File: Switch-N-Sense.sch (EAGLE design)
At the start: 40 parts, among them Q1 ZXMP10A13F, Q2 FDMT80080DC, Q3 FDMT80080DC, Q4 FDMT80080DC, Q5 FDMT80080DC, U1 BQ76200

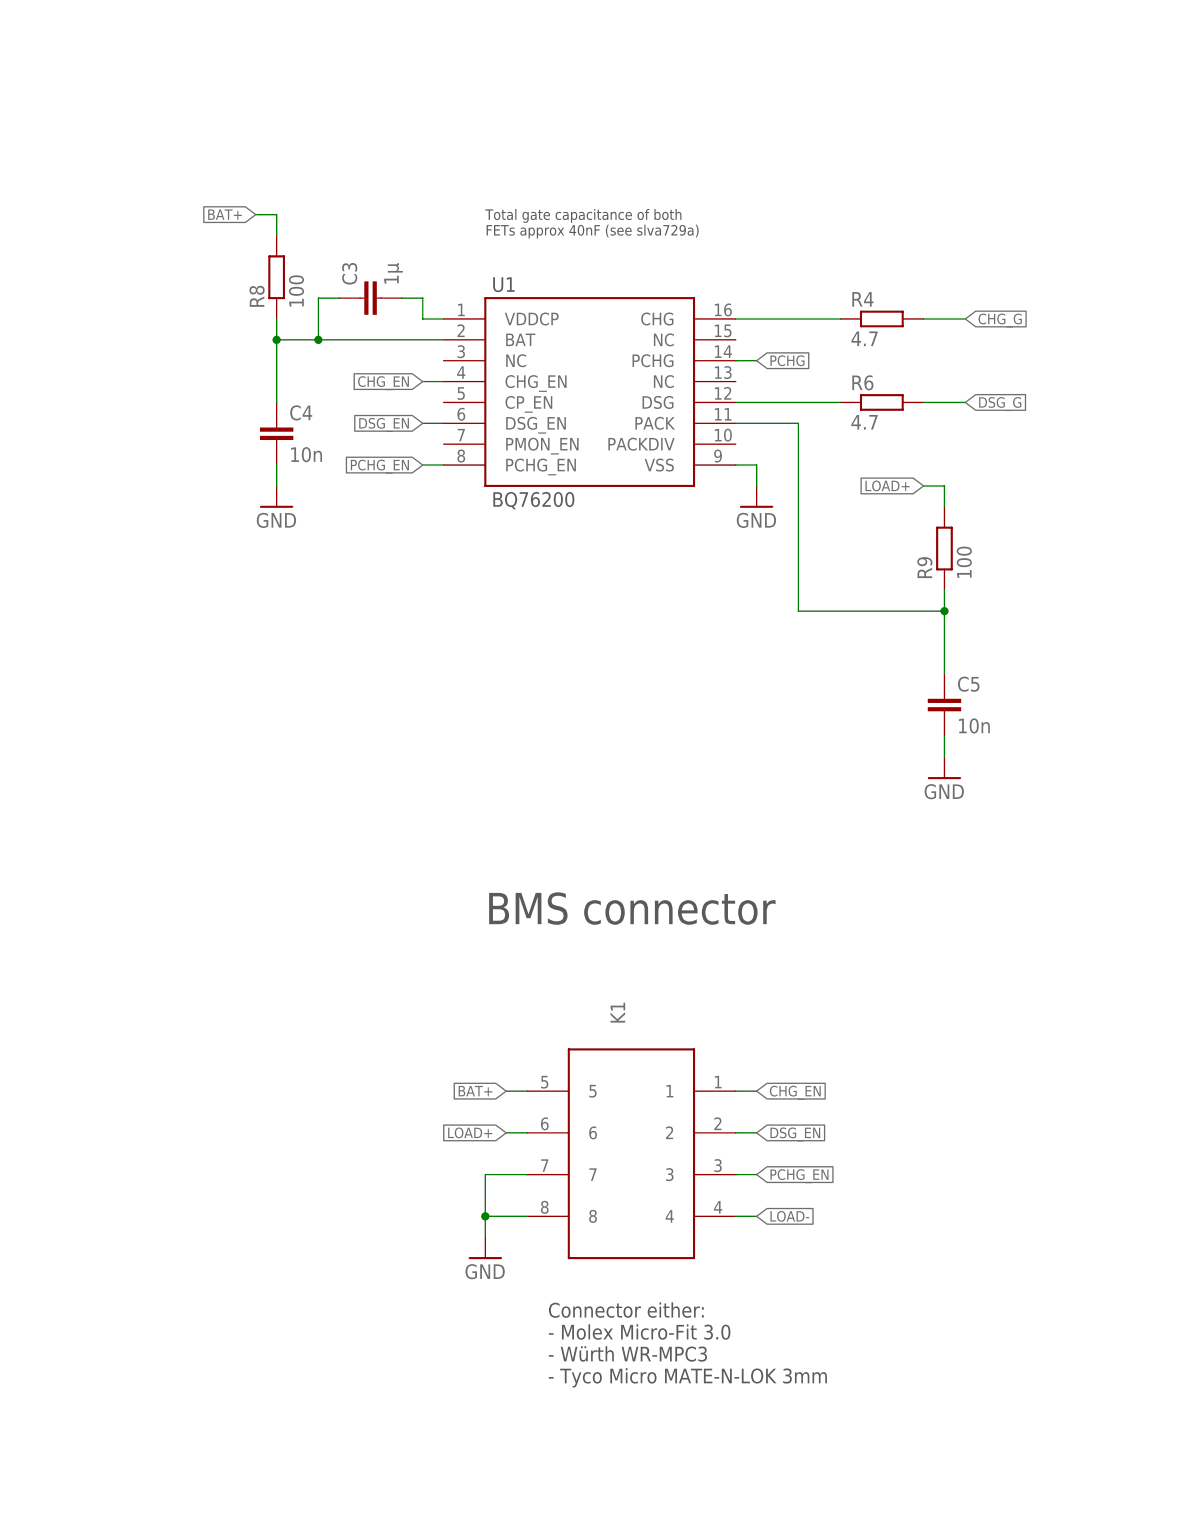
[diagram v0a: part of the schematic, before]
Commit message: Update to mate with new LibreSolar BMS48V
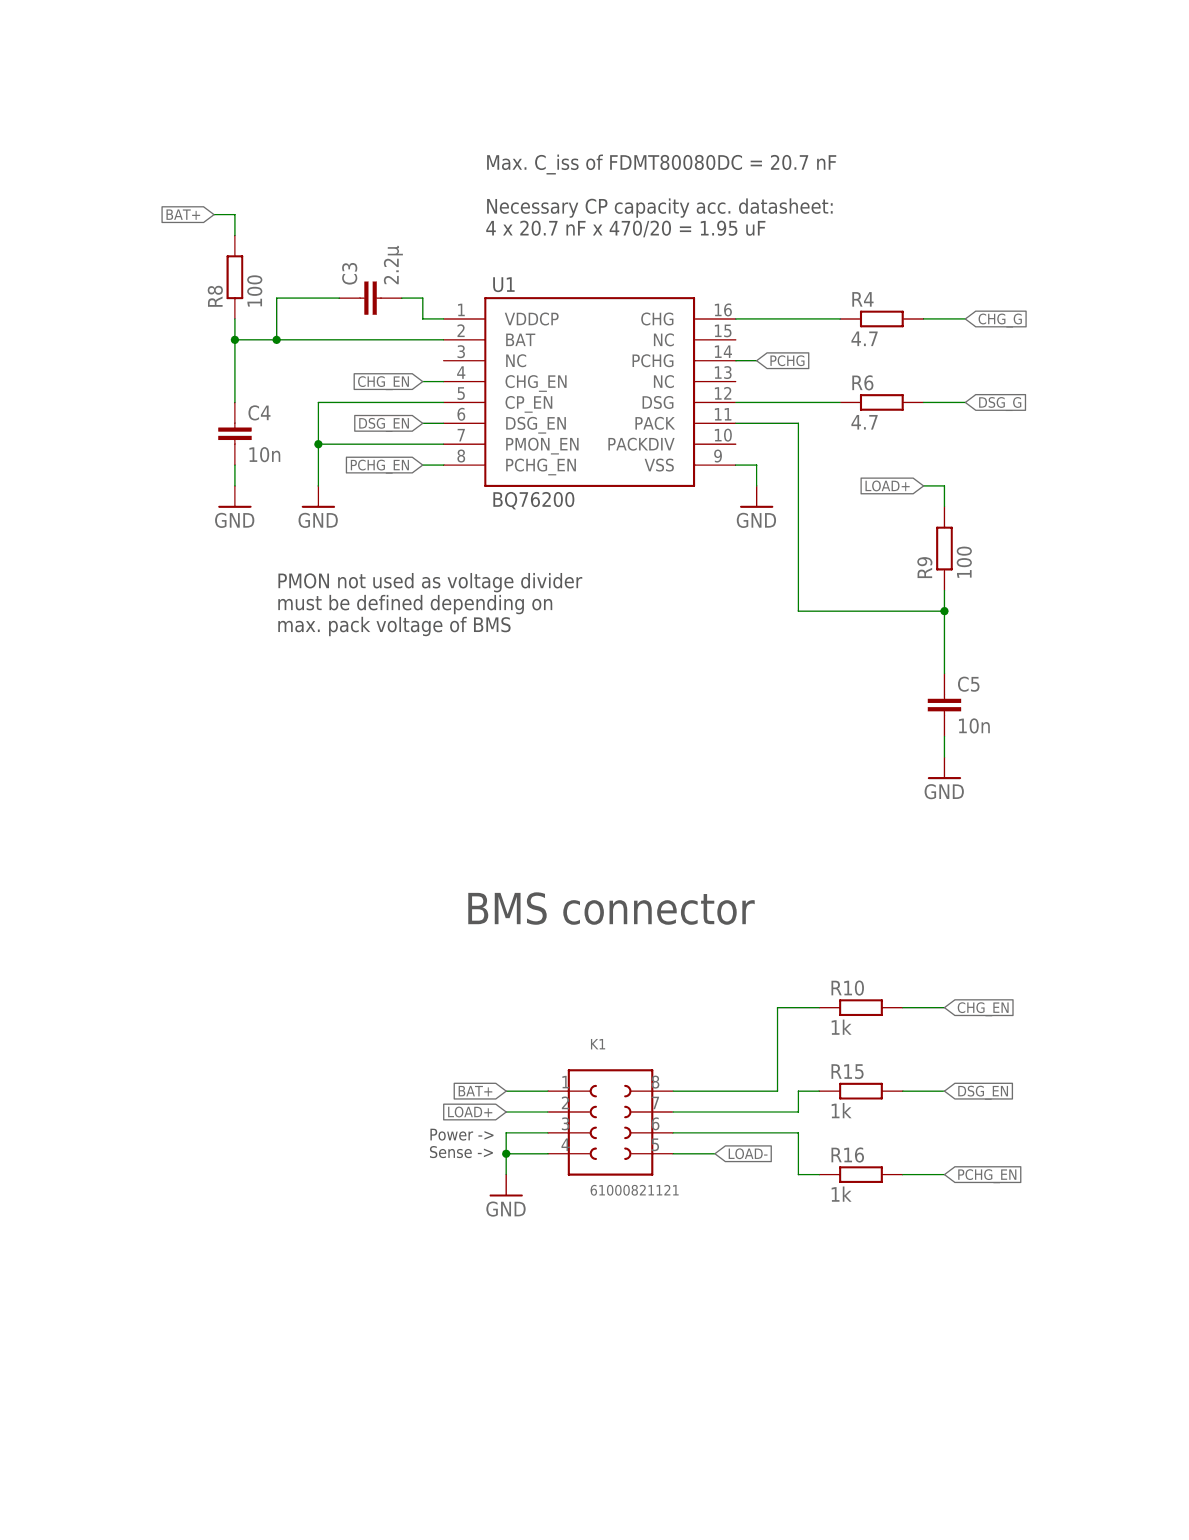
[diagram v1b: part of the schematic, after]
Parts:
- added R10, R15, R16: 1k, rcl:R-EU_R0603
- C3: value 1µ -> 2.2µ
- K1: value (none) -> 61000821121; device Wire_to_Board_Connectors_rev15d:662008231822 -> Board_to_Board_Connectors_rev15d:61000821121
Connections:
- new net N$4: K1.7, R15.1
- new net N$5: K1.6, R16.1
- new net N$6: K1.8, R10.1
- net BAT+: now also K1.1; no longer K1.5
- net CHG_EN: now also R10.2; no longer K1.1
- net DSG_EN: now also R15.2; no longer K1.2
- net GND: now also K1.3, K1.4, U1.CP_EN, U1.PMON_EN; no longer K1.7, K1.8
- net LOAD+: now also K1.2; no longer K1.6
- net LOAD-: now also K1.5; no longer K1.4
- net PCHG_EN: now also R16.2; no longer K1.3
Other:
- note added: "Max. C_iss of FDMT80080DC = 20.7 nF Necessary CP capacity acc. datasheet: 4 x 20.7 nF x 470/20 = 1.95 uF"
- note added: "PMON not used as voltage divider must be defined depending on max. pack voltage of BMS"
- note added: "Power -> Sense ->"
- note removed: "Connector either: - Molex Micro-Fit 3.0 - Würth WR-MPC3 - Tyco Micro MATE-N-LOK 3mm"
- note removed: "Total gate capacitance of both FETs approx 40nF (see slva729a)"
- moved on the sheet: C4, K1, R8
